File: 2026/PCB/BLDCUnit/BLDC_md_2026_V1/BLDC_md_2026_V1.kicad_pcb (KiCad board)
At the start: 2 copper layers, 40 x 51 mm, 86 parts, among them J1 Conn_01x07_Pin, J2 Conn_01x02_Pin, J3 Conn_01x03_Socket, J4 Conn_01x02_Socket, J5 Conn_01x06_Socket, SW1 SW_MEC_5E, SW2 SW_MEC_5E, U1 MAX3051

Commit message: ビミョいのでUNDO
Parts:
- moved JP2 1.82 mm to (228.9, 80.5), turned to -90 degrees
- moved JP1 1.73 mm to (231.4, 80.5), turned to -90 degrees
- moved C1 0.46 mm to (214.4, 90.8)
- moved C19 0.46 mm to (216.4, 90.8)
- moved C2 0.46 mm to (213.3, 90.8)
- moved C20 0.46 mm to (218.4, 90.8)
- moved C25 0.46 mm to (226.2, 85.3)
- moved C26 0.46 mm to (226.2, 86.3)
- moved C27 0.46 mm to (222.4, 90.8)
- moved C3 0.46 mm to (226.2, 81.2)
- moved C5 0.46 mm to (211.1, 87.5)
- moved C6 0.46 mm to (211.0, 80.1)
- moved C8 0.46 mm to (211.1, 90.5)
- moved C9 0.46 mm to (211.1, 89.0)
- moved MCU1 0.46 mm to (218.7, 83.5)
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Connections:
- R12 pad 1: GHS1 -> GHS3
- R13 pad 1: GLS1 -> GLS3
- R16 pad 1: GHS3 -> GHS1
- R17 pad 1: GLS3 -> GLS1
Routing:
- net BOOT1: track 0.00 -> 16.5 mm, vias 0 -> 2
- net BLDC_U: track 7.37 -> 22.1 mm, vias 14 -> 16
- net GLS3: track 0.00 -> 12.2 mm
- net GHS1: track 0.00 -> 11.6 mm
- net GHS3: track 0.00 -> 9.27 mm, vias 0 -> 2
- net GLS2: track 0.00 -> 8.48 mm, vias 0 -> 2
- net BOOT2: track 0.00 -> 7.67 mm, vias 0 -> 2
- net BLDC_W: track 7.47 -> 14.8 mm
- net USART_TX: track 0.00 -> 6.91 mm, vias 0 -> 1
- net GHS2: track 0.00 -> 5.43 mm
- net BOOT3: track 0.00 -> 5.39 mm
- net USART_RX: track 0.00 -> 5.21 mm, vias 0 -> 1
- net CAN_TX: track 0.00 -> 4.43 mm, vias 0 -> 2
- net CAN_RX: track 0.00 -> 4.27 mm, vias 0 -> 2
- net BLDC_V: track 7.37 -> 10.3 mm, vias 14 -> 15
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
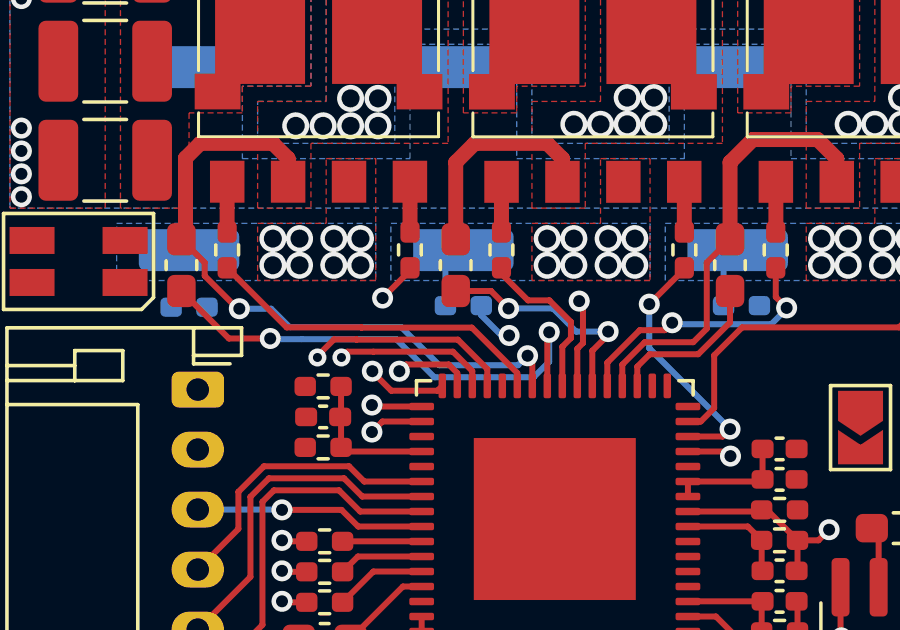
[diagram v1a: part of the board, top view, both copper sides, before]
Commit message: FET周りPCB配線
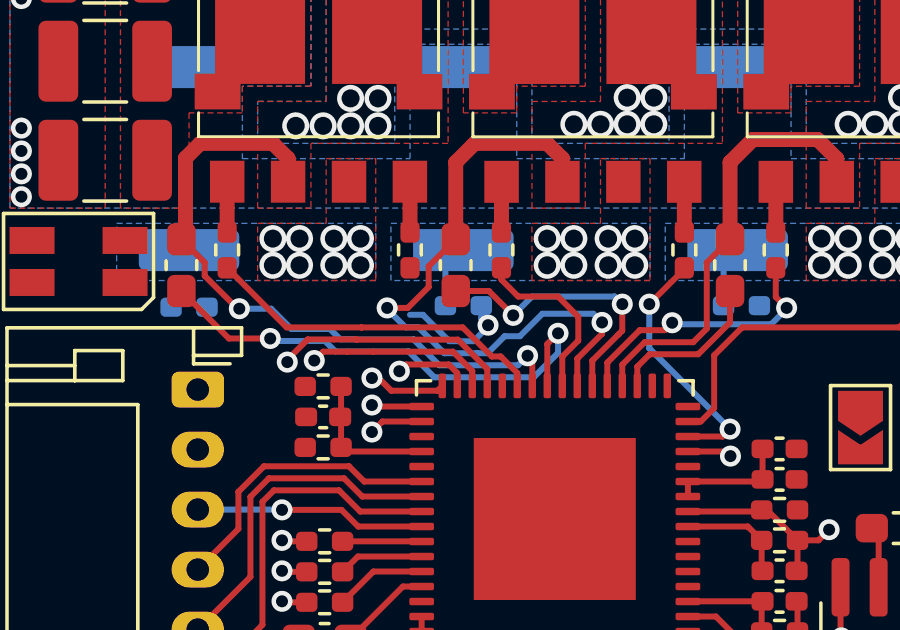
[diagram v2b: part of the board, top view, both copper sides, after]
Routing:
- net BLDC_V: track 10.3 -> 21.9 mm, vias 15 -> 16
- net OP2_VINP: track 1.53 -> 3.96 mm
- net BOOT2: track 7.67 -> 9.39 mm
- net GLS1: track 2.87 -> 1.57 mm, vias 2 -> 1
- net USART_TX: track 6.91 -> 7.99 mm
- net USART_RX: track 5.21 -> 6.15 mm
- net GHS2: track 5.43 -> 5.99 mm

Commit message: ん、詰んだ　Undoする
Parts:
- moved C6 1.07 mm to (209.9, 80.1)
- moved R1 1.07 mm to (209.9, 79.1)
- moved R2 1.07 mm to (209.9, 81.1)
- turned R32 to 180 degrees
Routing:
- net GLS1: track 1.57 -> 5.27 mm, vias 1 -> 2
- net BLDC_V: track 21.9 -> 24.5 mm
- net CAN_RX: track 4.27 -> 6.77 mm
- net OP2_VINP: track 3.96 -> 5.87 mm, vias 1 -> 0
- net CAN_TX: track 4.34 -> 5.85 mm
- net /Low_Side_Current_Sense2/SHUNT_P: track 0.84 -> 2.15 mm
- net Net-(MCU1-SCREF): track 4.78 -> 5.84 mm
- net BLDC_U: track 22.1 -> 23.0 mm
- net USART_TX: track 7.99 -> 7.18 mm
- net SSWCLK: track 1.80 -> 1.11 mm
- net BOOT1: track 16.6 -> 17.3 mm
- net USART_RX: track 6.15 -> 5.56 mm
- net SWDIO: track 1.68 -> 2.23 mm

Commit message: ん、FET周辺の配線終わり
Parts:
- moved C5 0.76 mm to (211.1, 88.3)
- moved C8 0.76 mm to (211.1, 91.3)
- moved C9 0.76 mm to (211.1, 89.8)
- moved R5 0.76 mm to (211.1, 85.0)
- moved R6 0.76 mm to (211.1, 86.1)
- moved R7 0.76 mm to (211.1, 87.1)
- moved C6 0.46 mm to (209.9, 80.6)
- moved R1 0.46 mm to (209.9, 79.6)
- moved R2 0.46 mm to (209.9, 81.6)
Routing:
- net USW: track 0.00 -> 8.55 mm, vias 0 -> 1
- net NRST: track 0.00 -> 8.55 mm, vias 0 -> 1
- net OP2_VINP: track 5.87 -> 10.7 mm, vias 0 -> 2
- net GLS1: track 5.27 -> 8.17 mm
- net SPI1_MOSI: track 12.9 -> 11.9 mm
- net SPI1_MISO: track 11.4 -> 10.4 mm
- net +8V: track 5.07 -> 6.00 mm
- net SPI1_SCK: track 9.83 -> 8.96 mm
- net +50V: track 3.09 -> 3.86 mm
- net GHS1: track 11.9 -> 12.6 mm, vias 0 -> 2

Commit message: 80%くらい配線完了
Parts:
- moved JP2 2.45 mm to (230.2, 78.4), turned to 180 degrees
- moved JP1 1.34 mm to (230.2, 80.9), turned to 180 degrees
- moved D1 0.40 mm to (235.9, 87.9)
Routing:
- net GLS1: track 8.17 -> 56.2 mm
- net OP2_VINP: track 10.7 -> 56.9 mm, vias 2 -> 3
- net OP1_VINP: track 0.00 -> 43.2 mm, vias 0 -> 3
- net Net-(D1-K): track 0.00 -> 32.9 mm, vias 0 -> 2
- net +8V: track 6.00 -> 38.2 mm
- net Net-(D5-A): track 0.00 -> 27.4 mm, vias 0 -> 2
- net Net-(D2-RA): track 0.84 -> 27.5 mm, vias 1 -> 2
- net Net-(D2-GA): track 0.84 -> 27.5 mm, vias 1 -> 2
- net Net-(D2-BA): track 0.84 -> 26.8 mm, vias 1 -> 2
- net Net-(D6-A): track 0.00 -> 25.7 mm, vias 0 -> 2
- net USART_RX: track 5.52 -> 27.1 mm
- net JP2: track 3.59 -> 24.2 mm, vias 0 -> 2
- net SWDIO: track 2.23 -> 21.6 mm
- net JP1: track 3.46 -> 22.8 mm, vias 0 -> 2
- net USART_TX: track 7.32 -> 24.2 mm
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
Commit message: 配線改良
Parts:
- R21, R22, R27, R32: moved to F.Cu
- moved R32 3.82 mm to (209.8, 74.6), turned to -90 degrees
- moved R27 3.79 mm to (219.0, 74.6), turned to -90 degrees
- moved R22 3.68 mm to (228.1, 74.6), turned to -90 degrees
- moved R18 2.19 mm to (227.0, 71.1)
- moved R19 2.19 mm to (217.8, 71.1)
- moved R20 2.19 mm to (208.7, 71.1)
- moved R21 1.73 mm to (230.2, 91.5)
- moved C21 1.28 mm to (230.2, 82.6)
- moved U1 1.28 mm to (230.2, 87.0)
- moved REF** 1.00 mm to (236.0, 55.0)
- moved REF** 1.00 mm to (204.0, 55.0)
- moved JP1 0.90 mm to (230.2, 80.0), turned to 0 degrees
- moved JP2 0.90 mm to (230.2, 77.5), turned to 0 degrees
- moved J2 0.89 mm to (213.6, 58.2)
- moved J3 0.89 mm to (229.1, 58.2)
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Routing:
- net +3V3: track 21.5 -> 58.9 mm, vias 0 -> 4
- net GLS1: track 56.2 -> 19.6 mm
- net OP2_VINP: track 56.9 -> 20.8 mm, vias 3 -> 2
- net +50V: track 17.5 -> 42.4 mm, vias 3 -> 2
- net USW: track 8.55 -> 32.5 mm, vias 1 -> 2
- net NRST: track 24.6 -> 39.5 mm
- net Net-(D5-A): track 27.4 -> 41.4 mm
- net Net-(D6-A): track 25.7 -> 36.9 mm
- net Net-(D2-BA): track 26.8 -> 17.5 mm
- net BLDC_V: track 24.5 -> 15.1 mm, vias 16 -> 14
- net Net-(D2-GA): track 27.5 -> 18.3 mm
- net JP2: track 24.2 -> 33.1 mm, vias 2 -> 4
- net CAN_TX: track 19.5 -> 28.2 mm
- net JP1: track 22.8 -> 30.0 mm, vias 2 -> 4
- net Net-(D2-RA): track 27.5 -> 21.3 mm
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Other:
- board size 40 x 51 mm -> 40 x 50 mm

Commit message: 配線完了
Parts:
- moved D1 2.46 mm to (237.9, 89.4), turned to -90 degrees
- moved C12 1.12 mm to (234.2, 90.5), turned to 90 degrees
- moved C11 1.01 mm to (235.7, 90.5), turned to 90 degrees
- moved R10 0.46 mm to (220.9, 90.7)
- moved R11 0.46 mm to (221.9, 90.7)
- moved C27 0.46 mm to (222.9, 90.7)
- moved R33 0.46 mm to (224.9, 90.8)
- moved R36 0.46 mm to (223.9, 90.8)
- moved C25 0.13 mm to (226.1, 85.3)
- moved C26 0.13 mm to (226.1, 86.3)
- moved C3 0.13 mm to (226.1, 81.2)
- moved C4 0.13 mm to (226.1, 82.2)
- moved R23 0.13 mm to (226.1, 83.2)
- moved R26 0.13 mm to (226.1, 84.2)
- moved R28 0.13 mm to (226.1, 88.3)
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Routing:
- net +3V3: track 58.9 -> 102.6 mm, vias 4 -> 3
- net GND: track 2.06 -> 18.1 mm, vias 48 -> 64
- net Net-(D5-A): track 41.4 -> 29.2 mm
- net Net-(D6-A): track 36.9 -> 28.4 mm
- net CAN_RX: track 25.6 -> 32.8 mm
- net +50V: track 42.4 -> 48.4 mm, vias 2 -> 3
- net +8V: track 40.3 -> 34.4 mm, vias 1 -> 2
- net JP1: track 30.0 -> 34.4 mm, vias 4 -> 2
- net Net-(D1-K): track 36.2 -> 32.9 mm, vias 3 -> 2
- net NRST: track 39.5 -> 36.8 mm
- net USW: track 32.5 -> 34.3 mm
- net OP3_VINP: track 12.4 -> 14.0 mm, vias 2 -> 4
- net OP1_VINP: track 46.9 -> 45.5 mm, vias 4 -> 2
- net OP2_VINP: track 20.8 -> 22.3 mm, vias 2 -> 4
- net JP2: track 33.1 -> 34.5 mm, vias 4 -> 2
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
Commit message: ん、DRC完了。問題ない
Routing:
- net GND: vias 64 -> 65
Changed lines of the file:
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@@
+	)
+	(via
+		(at 221.778 85.358)
+		(size 0.7)
+		(drill 0.4)
+		(layers "F.Cu" "B.Cu")
+		(free yes)
+		(net 1)
 	)
 	(via
